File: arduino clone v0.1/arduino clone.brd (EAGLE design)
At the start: 86.3 x 27.6 mm, 47 parts, among them J203 ICSP HEADER, J402 FTDI Breakout Header, U101 ATMEGA328P_TQFP, U301 CH340G, Y101 16MHz, Y301 12MHz

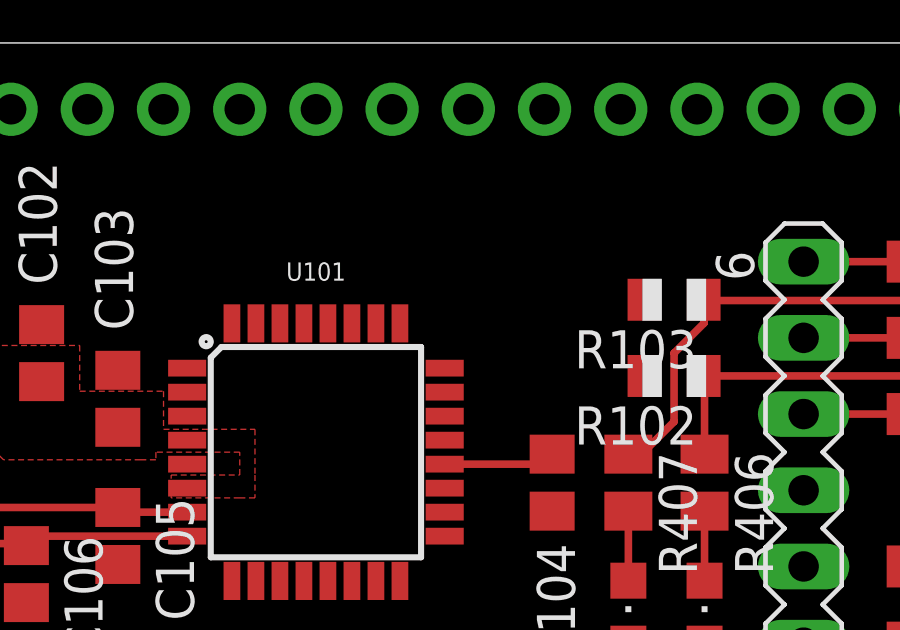
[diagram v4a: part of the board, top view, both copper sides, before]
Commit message: route UART RX and TX lines to MCU
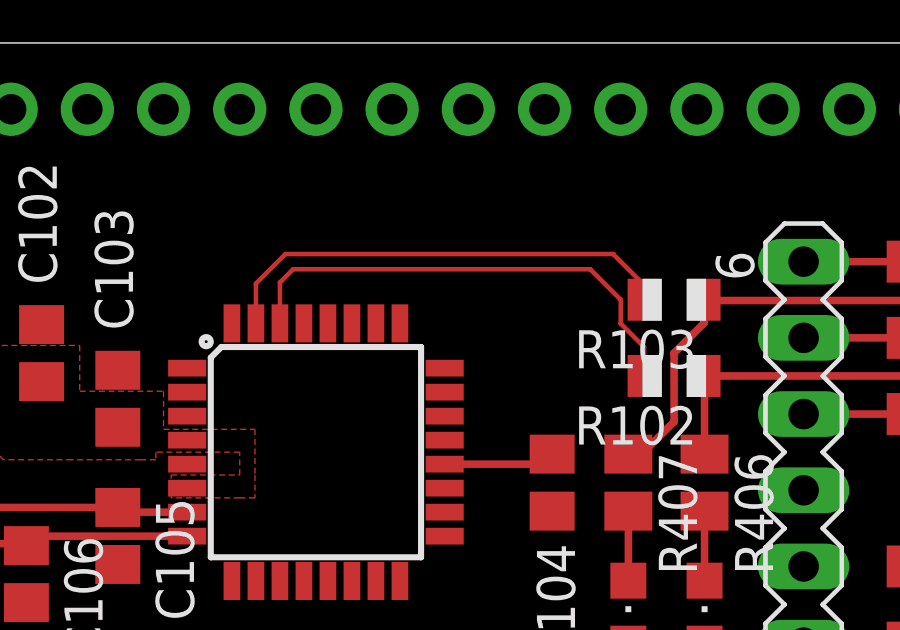
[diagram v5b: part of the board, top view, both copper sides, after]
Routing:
- net MCU_D0: track 0.00 -> 16.2 mm
- net MCU_D1: track 0.00 -> 15.6 mm
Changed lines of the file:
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@@
 <setting verticaltext="up"/>
 </settings>
-<grid distance="50" unitdist="mil" unit="mil" style="lines" multiple="1" display="yes" altdistance="5" altunitdist="mil" altunit="mil"/>
+<grid distance="10" unitdist="mil" unit="mil" style="lines" multiple="1" display="yes" altdistance="5" altunitdist="mil" altunit="mil"/>
 <layers>
 <layer number="1" name="Top" color="4" fill="1" visible="yes" active="yes"/>
@@
 </element>
 <element name="U101" library="SparkFun-IC-Microcontroller" package="TQFP32-08" value="ATMEGA328P_TQFP" x="34.29" y="52.07" smashed="yes">
-<attribute name="NAME" x="34.29" y="57.785" size="0.6096" layer="25" font="vector" ratio="20" align="bottom-center"/>
 <attribute name="PROD_ID" value="IC-09069" x="34.29" y="52.07" size="1.778" layer="27" display="off"/>
 <attribute name="VALUE" x="34.29" y="45.72" size="0.6096" layer="27" font="vector" ratio="20" align="bottom-center"/>
@@
 <contactref element="R103" pad="2"/>
 <contactref element="J201" pad="1"/>
-<wire x1="32.29" y1="56.3626" x2="45.228" y2="57.15" width="0" layer="19" extent="1-1"/>
+<wire x1="32.29" y1="56.3626" x2="32.29" y2="57.69" width="0.1524" layer="1"/>
+<wire x1="32.29" y1="57.69" x2="33.274" y2="58.674" width="0.1524" layer="1"/>
+<wire x1="33.274" y1="58.674" x2="44.196" y2="58.674" width="0.1524" layer="1"/>
+<wire x1="44.196" y1="58.674" x2="45.228" y2="57.642" width="0.1524" layer="1"/>
+<wire x1="45.228" y1="57.642" x2="45.228" y2="57.15" width="0.1524" layer="1"/>
 <wire x1="24.13" y1="40.64" x2="32.29" y2="56.3626" width="0" layer="19" extent="1-1"/>
 </signal>
@@
 <contactref element="R102" pad="2"/>
 <contactref element="J201" pad="2"/>
-<wire x1="33.09" y1="56.3626" x2="45.228" y2="54.61" width="0" layer="19" extent="1-1"/>
+<wire x1="33.09" y1="56.3626" x2="33.09" y2="57.728" width="0.1524" layer="1"/>
+<wire x1="33.09" y1="57.728" x2="33.528" y2="58.166" width="0.1524" layer="1"/>
+<wire x1="43.434" y1="58.166" x2="44.4494" y2="57.1506" width="0.1524" layer="1"/>
+<wire x1="44.4494" y1="57.1506" x2="44.4494" y2="56.3553125" width="0.1524" layer="1"/>
+<wire x1="45.228" y1="55.5767125" x2="45.228" y2="54.61" width="0.1524" layer="1"/>
+<wire x1="44.4494" y1="56.3553125" x2="45.228" y2="55.5767125" width="0.1524" layer="1"/>
+<wire x1="33.528" y1="58.166" x2="43.434" y2="58.166" width="0.1524" layer="1"/>
 <wire x1="26.67" y1="40.64" x2="33.09" y2="56.3626" width="0" layer="19" extent="1-1"/>
 </signal>

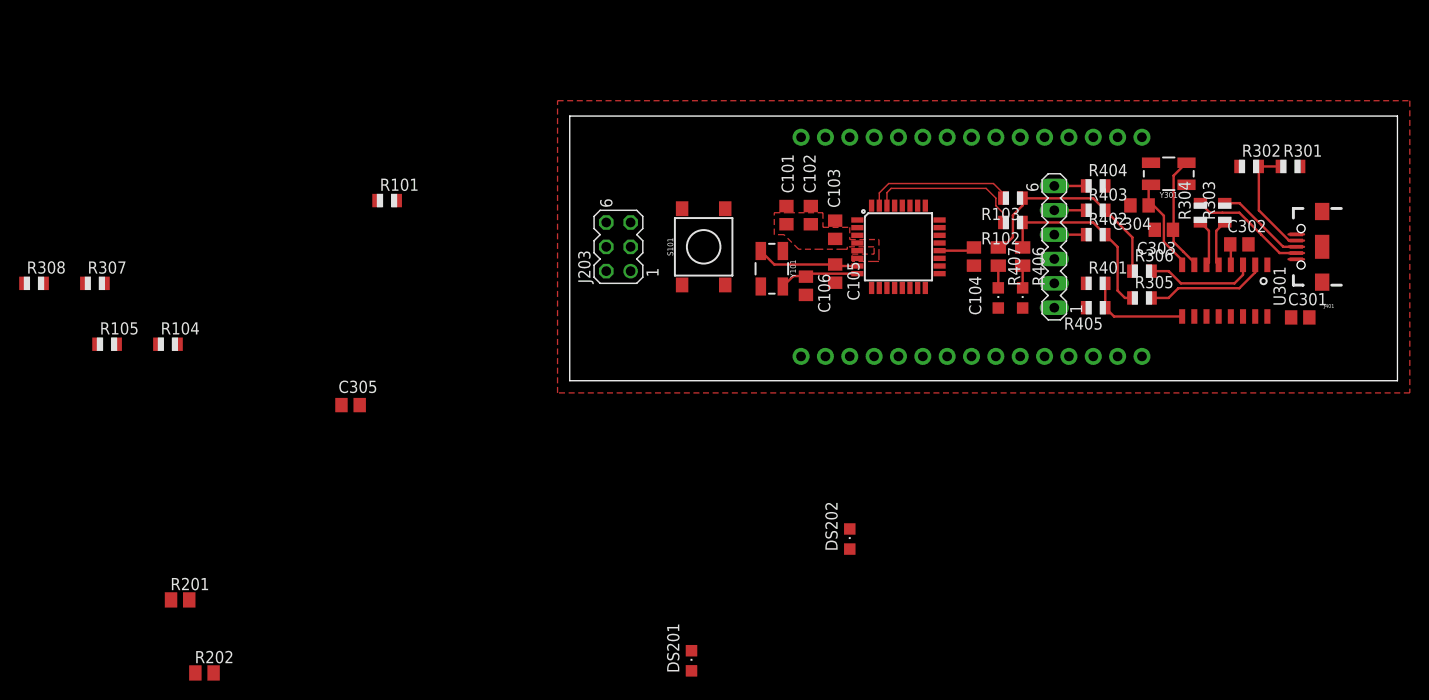
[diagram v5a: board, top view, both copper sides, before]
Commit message: place and route power indicator LED
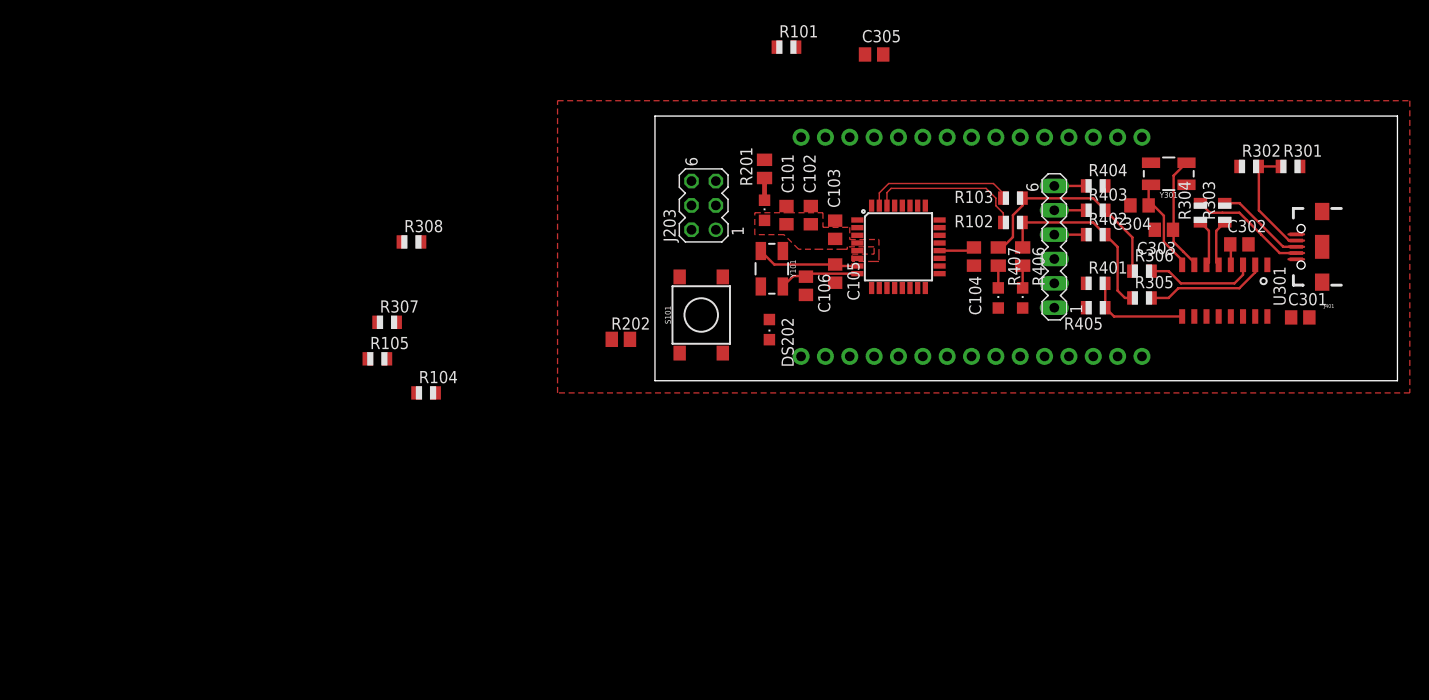
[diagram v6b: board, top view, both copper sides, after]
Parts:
- moved R201 75.7 mm to (20.3, 60.2), turned to 270 degrees
- moved C305 65.7 mm to (31.8, 72.1)
- moved R202 55.7 mm to (5.33, 42.4)
- moved DS201 47.6 mm to (20.3, 55.9)
- moved R101 44.6 mm to (22.6, 72.9)
- moved R308 39.6 mm to (-16.5, 52.6)
- moved R307 30.7 mm to (-19.1, 44.2)
- moved R105 28.2 mm to (-20.1, 40.4)
- moved R104 27.4 mm to (-15.0, 36.8)
- moved DS202 23.4 mm to (20.8, 43.4), turned to 180 degrees
- moved J203 9.88 mm to (14.0, 56.4)
- moved S101 7.12 mm to (13.7, 45.0)
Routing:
- net LED_DS201: track 0.00 -> 2.32 mm
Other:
- board size 86.3 x 27.6 mm -> 77.5 x 27.6 mm

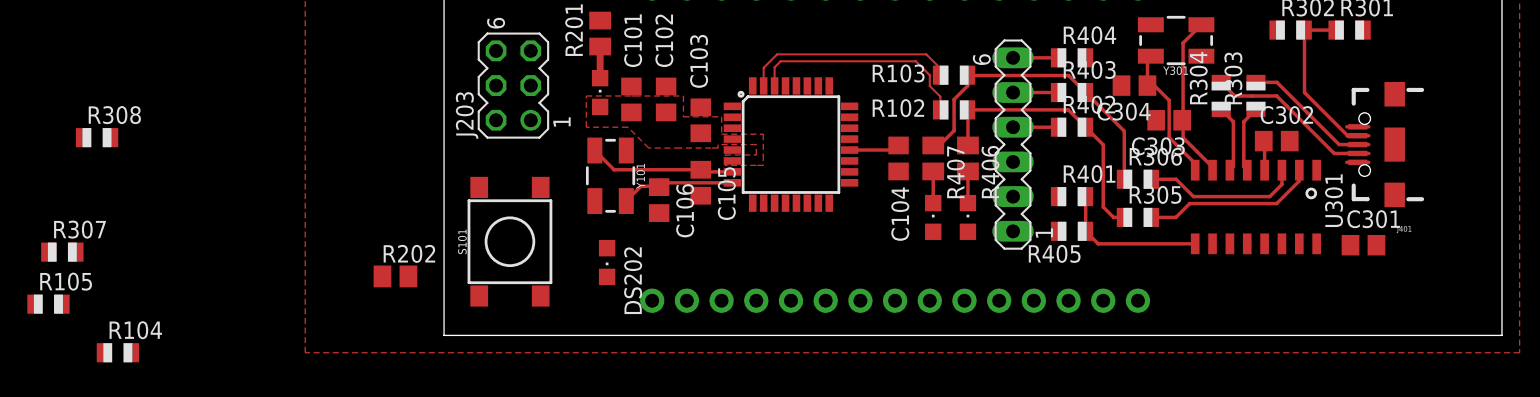
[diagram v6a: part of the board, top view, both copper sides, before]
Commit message: place CH340G power series reisistor
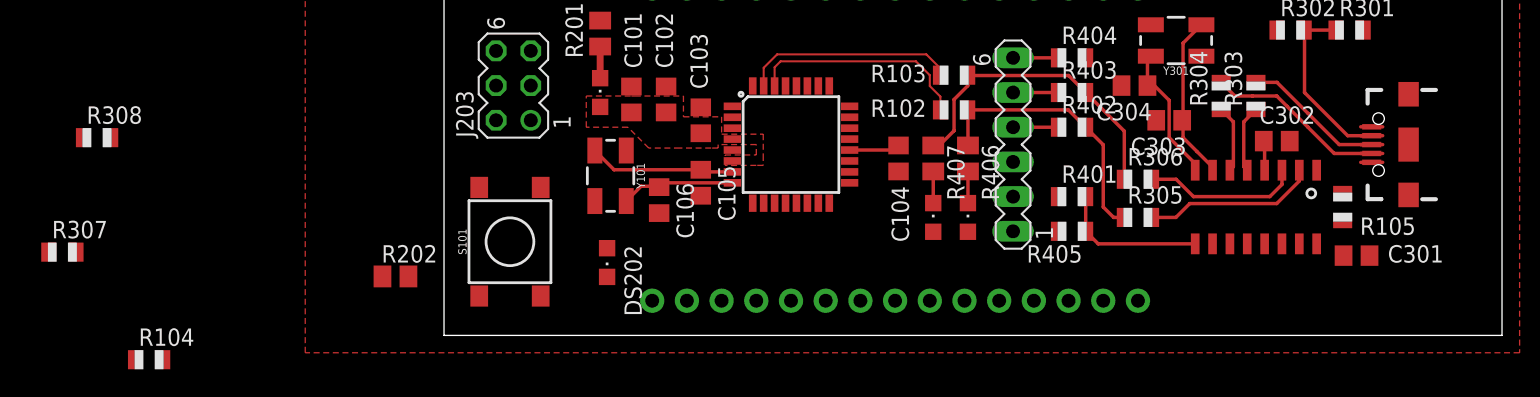
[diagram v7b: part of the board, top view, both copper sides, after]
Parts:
- moved R105 95.0 mm to (74.7, 47.5), turned to 90 degrees
- moved R104 2.34 mm to (-12.7, 36.3)
- moved J401 1.02 mm to (79.5, 52.1)
- moved C301 0.92 mm to (75.7, 43.9)
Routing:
- net USB_ID: track 12.1 -> 13.1 mm
- net USB_DAT_P: track 9.35 -> 10.4 mm
- net USB_DAT_N: track 12.2 -> 13.2 mm
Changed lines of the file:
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@@
 <attribute name="VALUE" x="22.098" y="49.276" size="1.27" layer="27" rot="R270"/>
 </element>
-<element name="C301" library="rcl" library_urn="urn:adsk.eagle:library:334" package="C0805" package3d_urn="urn:adsk.eagle:package:23617/2" value="0.1uF" x="76.2" y="44.704" smashed="yes">
-<attribute name="NAME" x="74.93" y="45.974" size="1.27" layer="25"/>
-<attribute name="SPICEPREFIX" value="C" x="76.2" y="44.704" size="1.778" layer="27" display="off"/>
-<attribute name="VALUE" x="74.93" y="42.164" size="1.27" layer="27"/>
+<element name="C301" library="rcl" library_urn="urn:adsk.eagle:library:334" package="C0805" package3d_urn="urn:adsk.eagle:package:23617/2" value="0.1uF" x="75.692" y="43.942" smashed="yes">
+<attribute name="NAME" x="77.978" y="43.434" size="1.27" layer="25"/>
+<attribute name="SPICEPREFIX" value="C" x="75.692" y="43.942" size="1.778" layer="27" display="off"/>
 </element>
 <element name="C302" library="rcl" library_urn="urn:adsk.eagle:library:334" package="C0805" package3d_urn="urn:adsk.eagle:package:23617/2" value="10nF" x="69.85" y="52.324" smashed="yes">
@@
 <attribute name="OC_NEWARK" value="unknown" x="13.97" y="56.388" size="1.778" layer="27" rot="R90" display="off"/>
 </element>
-<element name="J401" library="Testing" package="USB-AB-MICRO-SMD-V03-IN&amp;OUT" value="" x="78.486" y="52.07" smashed="yes" rot="R180">
-<attribute name="NAME" x="79.756" y="46.101" size="0.4064" layer="25" rot="R180"/>
-<attribute name="VALUE" x="79.756" y="46.609" size="0.4064" layer="27" rot="R180"/>
+<element name="J401" library="Testing" package="USB-AB-MICRO-SMD-V03-IN&amp;OUT" value="" x="79.502" y="52.07" smashed="yes" rot="R180">
+<attribute name="VALUE" x="80.772" y="46.609" size="0.4064" layer="27" rot="R180"/>
 </element>
 <element name="J402" library="con-lstb" library_urn="urn:adsk.eagle:library:162" package="MA06-1" package3d_urn="urn:adsk.eagle:package:8340/1" value="FTDI Breakout Header" x="50.546" y="52.07" smashed="yes" rot="R90">
@@
 <attribute name="NAME" x="44.196" y="57.912" size="1.27" layer="25" rot="R180"/>
 </element>
-<element name="R104" library="adafruit" package="R0805" value="0" x="-14.986" y="36.83" smashed="yes">
-<attribute name="NAME" x="-15.748" y="37.846" size="1.27" layer="25"/>
-<attribute name="VALUE" x="-15.748" y="34.544" size="1.27" layer="27"/>
-</element>
-<element name="R105" library="adafruit" package="R0805" value="0" x="-20.066" y="40.386" smashed="yes">
-<attribute name="NAME" x="-20.828" y="41.402" size="1.27" layer="25"/>
-<attribute name="VALUE" x="-20.828" y="38.1" size="1.27" layer="27"/>
+<element name="R104" library="adafruit" package="R0805" value="0" x="-12.7" y="36.322" smashed="yes">
+<attribute name="NAME" x="-13.462" y="37.338" size="1.27" layer="25"/>
+</element>
+<element name="R105" library="adafruit" package="R0805" value="0" x="74.676" y="47.498" smashed="yes" rot="R90">
+<attribute name="NAME" x="75.946" y="45.466" size="1.27" layer="25"/>
 </element>
 <element name="R301" library="adafruit" package="R0805" value="10k" x="75.184" y="60.452" smashed="yes">
@@
 <attribute name="VALUE" x="34.29" y="45.72" size="0.6096" layer="27" font="vector" ratio="20" align="bottom-center"/>
 </element>
-<element name="U301" library="my-eagle-lib" package="SOIC16" value="CH340G" x="68.326" y="47.498" smashed="yes" rot="R180">
-<attribute name="NAME" x="73.406" y="50.038" size="1.27" layer="25" rot="R270"/>
-</element>
+<element name="U301" library="my-eagle-lib" package="SOIC16" value="CH340G" x="68.326" y="47.498" smashed="yes" rot="R180"/>
 <element name="Y101" library="SparkFun-Clocks" package="CRYSTAL-SMD-5X3.2-4PAD" value="16MHz" x="21.082" y="49.784" smashed="yes" rot="R270">
 <attribute name="NAME" x="22.987" y="49.784" size="0.6096" layer="25" font="vector" ratio="20" rot="R270" align="bottom-center"/>
@@
 <wire x1="44.704" y1="45.686" x2="38.5826" y2="50.07" width="0" layer="19" extent="1-1"/>
 <wire x1="47.244" y1="45.686" x2="44.704" y2="45.686" width="0" layer="19" extent="1-1"/>
-<wire x1="-15.986" y1="36.83" x2="20.32" y2="54.83" width="0" layer="19" extent="1-1"/>
+<wire x1="-13.7" y1="36.322" x2="20.32" y2="54.83" width="0" layer="19" extent="1-1"/>
 </signal>
 <signal name="GND">
@@
 <vertex x="-1.27" y="36.83"/>
 </polygon>
-<wire x1="72.771" y1="50.193" x2="75.786" y2="53.37" width="0" layer="19" extent="1-1"/>
+<wire x1="72.771" y1="50.193" x2="76.802" y2="53.37" width="0" layer="19" extent="1-1"/>
 <wire x1="29.9974" y1="51.67" x2="29.9974" y2="53.27" width="0" layer="19" extent="1-1"/>
 <wire x1="4.384" y1="42.418" x2="15.966" y2="48.933" width="0" layer="19" extent="1-1"/>
@@
 <contactref element="J401" pad="VBUS1"/>
 <contactref element="J402" pad="3"/>
-<wire x1="75.786" y1="50.77" x2="76.184" y2="60.452" width="0" layer="19" extent="1-1"/>
+<wire x1="76.802" y1="50.77" x2="76.184" y2="60.452" width="0" layer="19" extent="1-1"/>
 <wire x1="57.15" y1="63.5" x2="76.184" y2="60.452" width="0" layer="19" extent="1-1"/>
 <wire x1="50.546" y1="50.8" x2="57.15" y2="63.5" width="0" layer="19" extent="1-1"/>
@@
 <wire x1="24.13" y1="63.5" x2="31.75" y2="63.5" width="0" layer="19" extent="1-1"/>
 <wire x1="12.7" y1="53.848" x2="24.13" y2="63.5" width="0" layer="19" extent="1-1"/>
-<wire x1="-13.986" y1="36.83" x2="12.7" y2="53.848" width="0" layer="19" extent="1-1"/>
-<wire x1="-19.066" y1="40.386" x2="-13.986" y2="36.83" width="0" layer="19" extent="1-1"/>
+<wire x1="-11.7" y1="36.322" x2="12.7" y2="53.848" width="0" layer="19" extent="1-1"/>
+<wire x1="74.676" y1="48.498" x2="-11.7" y2="36.322" width="0" layer="19" extent="1-1"/>
 </signal>
 <signal name="PP5V0_CH340G">
@@
 <contactref element="C301" pad="1"/>
 <contactref element="R307" pad="2"/>
-<wire x1="72.771" y1="44.803" x2="75.25" y2="44.704" width="0" layer="19" extent="1-1"/>
+<wire x1="74.742" y1="43.942" x2="72.771" y2="44.803" width="0" layer="19" extent="1-1"/>
 <wire x1="-18.05" y1="44.196" x2="72.771" y2="44.803" width="0" layer="19" extent="1-1"/>
-<wire x1="-21.066" y1="40.386" x2="-18.05" y2="44.196" width="0" layer="19" extent="1-1"/>
+<wire x1="74.676" y1="46.498" x2="-18.05" y2="44.196" width="0" layer="19" extent="1-1"/>
 </signal>
 <signal name="MCU_D14">
@@
 <contactref element="R304" pad="2"/>
 <contactref element="J401" pad="D-1"/>
-<wire x1="75.786" y1="51.42" x2="74.056" y2="51.42" width="0.254" layer="1"/>
+<wire x1="76.802" y1="51.42" x2="74.056" y2="51.42" width="0.254" layer="1"/>
 <wire x1="66.786" y1="55.626" x2="65.786" y2="56.626" width="0.254" layer="1"/>
 <wire x1="68.072" y1="55.626" x2="66.786" y2="55.626" width="0.254" layer="1"/>
@@
 <contactref element="J401" pad="ID1"/>
 <wire x1="71.866" y1="60.452" x2="74.184" y2="60.452" width="0.254" layer="1"/>
-<wire x1="75.786" y1="52.72" x2="75.042" y2="52.72" width="0.254" layer="1"/>
+<wire x1="76.802" y1="52.72" x2="75.042" y2="52.72" width="0.254" layer="1"/>
 <wire x1="75.042" y1="52.72" x2="71.882" y2="55.88" width="0.254" layer="1"/>
 <wire x1="71.882" y1="55.88" x2="71.882" y2="60.436" width="0.254" layer="1"/>
@@
 <contactref element="R303" pad="2"/>
 <contactref element="J401" pad="D+1"/>
-<wire x1="75.786" y1="52.07" x2="74.422" y2="52.07" width="0.254" layer="1"/>
+<wire x1="76.802" y1="52.07" x2="74.422" y2="52.07" width="0.254" layer="1"/>
 <wire x1="74.422" y1="52.07" x2="72.136" y2="54.356" width="0.254" layer="1"/>
 <wire x1="72.136" y1="54.356" x2="69.866" y2="56.626" width="0.254" layer="1"/>
